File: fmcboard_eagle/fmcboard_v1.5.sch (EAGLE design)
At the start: 176 parts, among them IC1 OPA699ID, IC10 LTC6229IMS8E#TRPBF, IC11 7805TV, IC12 SN74AUC2G66DCTR, IC13 SN74AUC2G66DCTR, IC14 SN74AUC2G66DCTR, IC15 SN74AUC2G66DCTR, IC16 DAC7578SPWR, IC17 SN74AUC2G66DCTR, IC18 SN74AUC2G66DCTR, IC19 SN74AUC2G66DCTR, IC2 DAC7578SPWR, IC20 SN74AUC2G66DCTR, IC21 74AUP2GU04GW,125, IC22 74AUP2GU04GW,125, IC23 74AUP2GU04GW,125, IC24 74AUP2GU04GW,125, IC25 LM358, IC3 LTC6229IMS8E#TRPBF, IC4 LTC6229IMS8E#TRPBF, IC6 OPA699ID, IC7 OPA699ID, IC8 LTC6229IMS8E#TRPBF, IC9 LTC6229IMS8E#TRPBF, J1 8pin, J10 8pin, J12 4p-2.54, J2 ASP-134604-01, J3 4p-2.54, J4 4p-2.54, J5 8pin, J6 4p-2.54, J7 4p-2.54, J8 4p-2.54, J9 8pin, U1 TXS0108EPWR, U2 STMICROELECTRONICS_L7905ACVST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

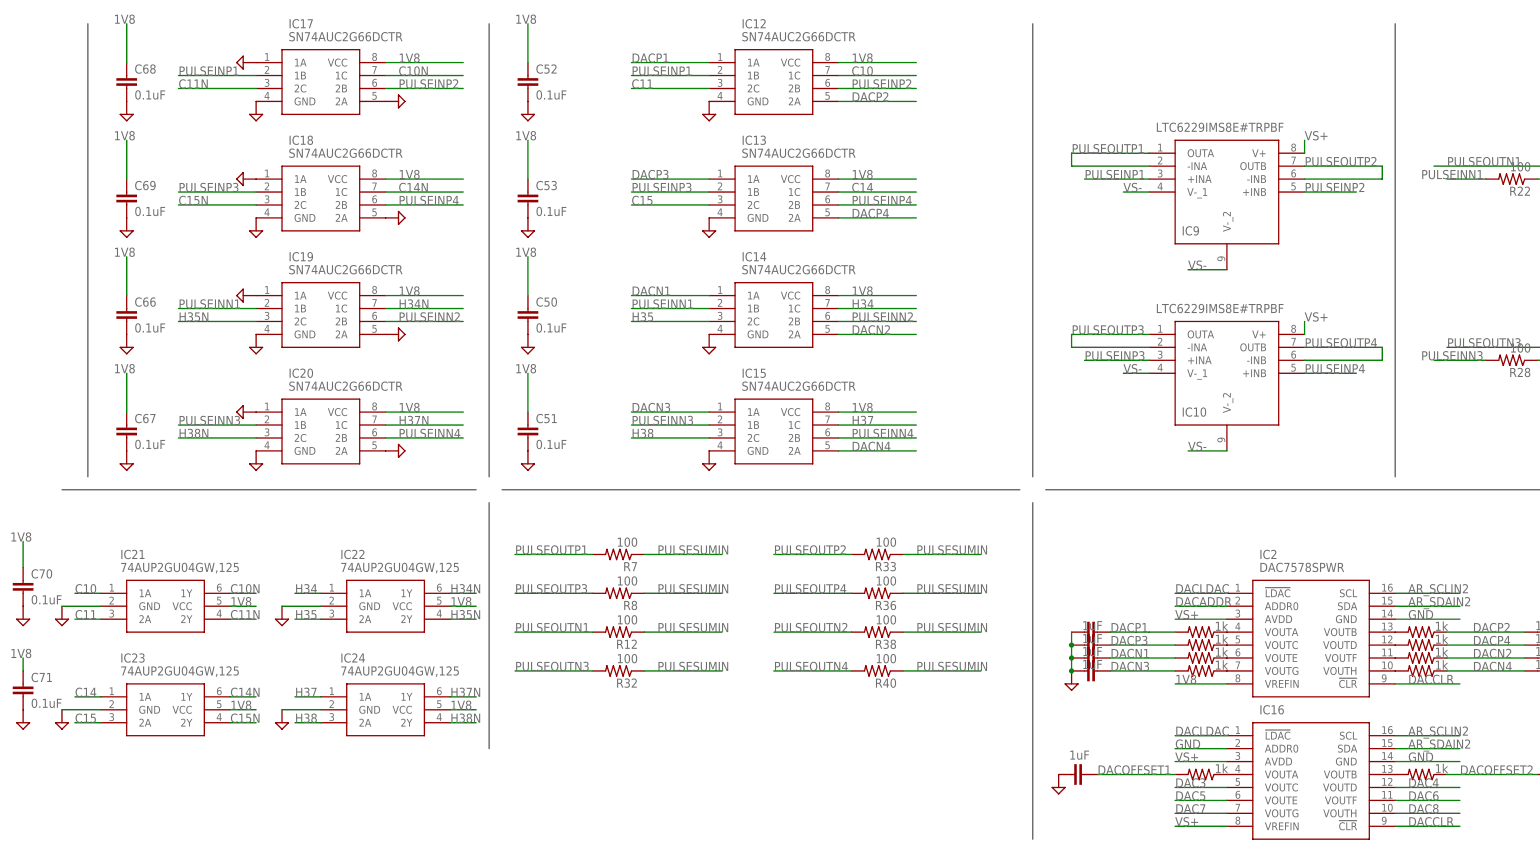
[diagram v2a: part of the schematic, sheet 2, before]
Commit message: 100 ohm between dac and caps
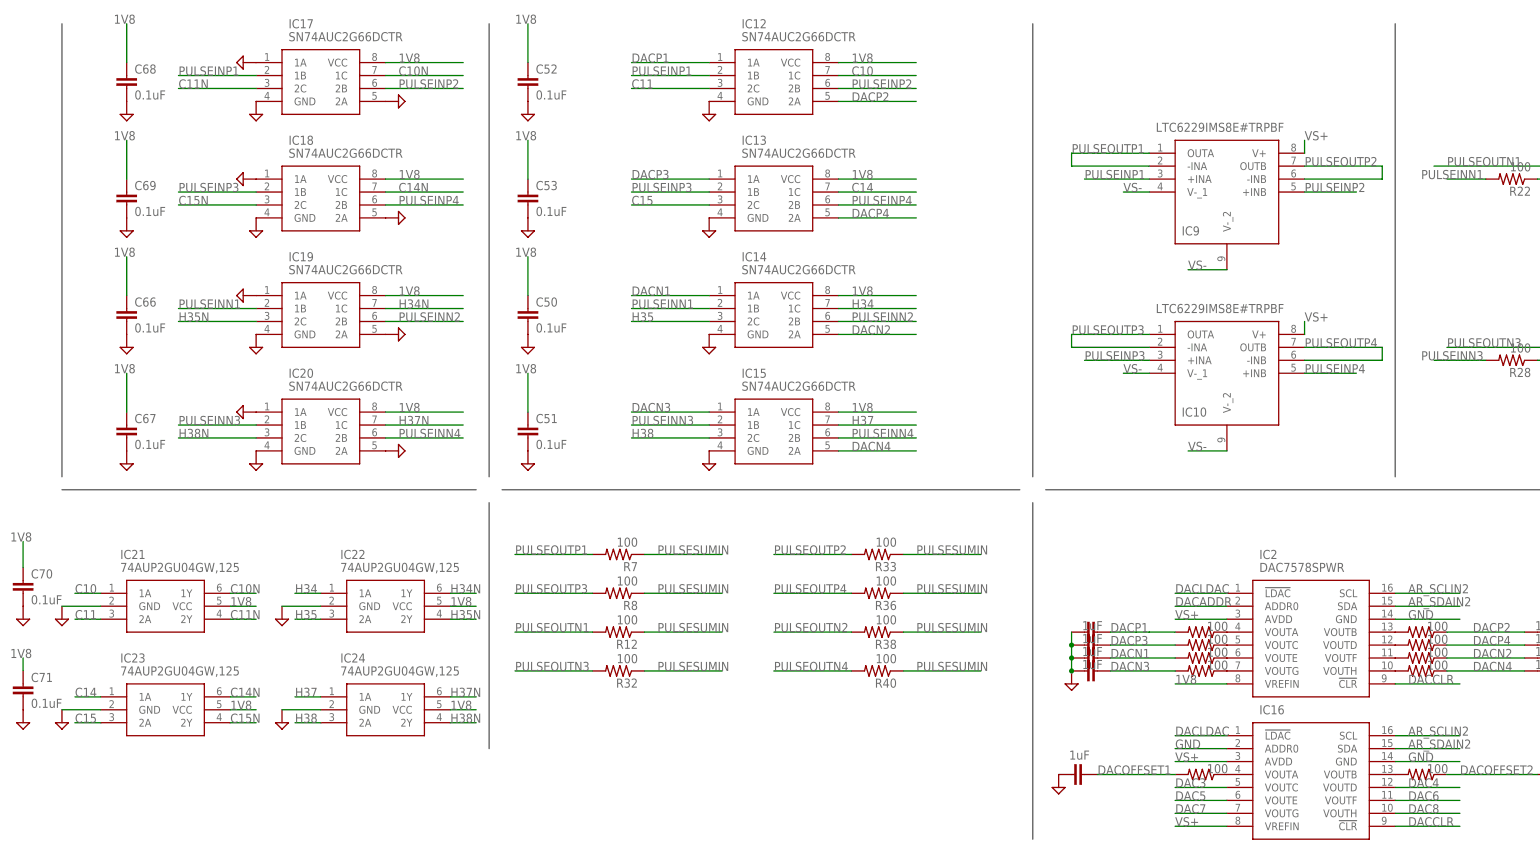
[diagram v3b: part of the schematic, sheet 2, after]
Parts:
- R47, R53, R54, R55, R56, R57, R58, R59, R60, R61: value 1k -> 100
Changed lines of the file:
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@@
 <part name="SUPPLY92" library="supply2" library_urn="urn:adsk.eagle:library:372" deviceset="GND" device=""/>
 <part name="IC25" library="SparkFun-IC-Amplifiers" library_urn="urn:adsk.eagle:library:520" deviceset="OPAMP-DUAL" device="U" package3d_urn="urn:adsk.eagle:package:38665/1" value="LM358"/>
-<part name="R47" library="rcl" library_urn="urn:adsk.eagle:library:334" deviceset="R-US_" device="R0805" package3d_urn="urn:adsk.eagle:package:23553/2" value="1k"/>
-<part name="R53" library="rcl" library_urn="urn:adsk.eagle:library:334" deviceset="R-US_" device="R0805" package3d_urn="urn:adsk.eagle:package:23553/2" value="1k"/>
-<part name="R54" library="rcl" library_urn="urn:adsk.eagle:library:334" deviceset="R-US_" device="R0805" package3d_urn="urn:adsk.eagle:package:23553/2" value="1k"/>
-<part name="R55" library="rcl" library_urn="urn:adsk.eagle:library:334" deviceset="R-US_" device="R0805" package3d_urn="urn:adsk.eagle:package:23553/2" value="1k"/>
-<part name="R56" library="rcl" library_urn="urn:adsk.eagle:library:334" deviceset="R-US_" device="R0805" package3d_urn="urn:adsk.eagle:package:23553/2" value="1k"/>
-<part name="R57" library="rcl" library_urn="urn:adsk.eagle:library:334" deviceset="R-US_" device="R0805" package3d_urn="urn:adsk.eagle:package:23553/2" value="1k"/>
-<part name="R58" library="rcl" library_urn="urn:adsk.eagle:library:334" deviceset="R-US_" device="R0805" package3d_urn="urn:adsk.eagle:package:23553/2" value="1k"/>
-<part name="R59" library="rcl" library_urn="urn:adsk.eagle:library:334" deviceset="R-US_" device="R0805" package3d_urn="urn:adsk.eagle:package:23553/2" value="1k"/>
-<part name="R60" library="rcl" library_urn="urn:adsk.eagle:library:334" deviceset="R-US_" device="R0805" package3d_urn="urn:adsk.eagle:package:23553/2" value="1k"/>
-<part name="R61" library="rcl" library_urn="urn:adsk.eagle:library:334" deviceset="R-US_" device="R0805" package3d_urn="urn:adsk.eagle:package:23553/2" value="1k"/>
+<part name="R47" library="rcl" library_urn="urn:adsk.eagle:library:334" deviceset="R-US_" device="R0805" package3d_urn="urn:adsk.eagle:package:23553/2" value="100"/>
+<part name="R53" library="rcl" library_urn="urn:adsk.eagle:library:334" deviceset="R-US_" device="R0805" package3d_urn="urn:adsk.eagle:package:23553/2" value="100"/>
+<part name="R54" library="rcl" library_urn="urn:adsk.eagle:library:334" deviceset="R-US_" device="R0805" package3d_urn="urn:adsk.eagle:package:23553/2" value="100"/>
+<part name="R55" library="rcl" library_urn="urn:adsk.eagle:library:334" deviceset="R-US_" device="R0805" package3d_urn="urn:adsk.eagle:package:23553/2" value="100"/>
+<part name="R56" library="rcl" library_urn="urn:adsk.eagle:library:334" deviceset="R-US_" device="R0805" package3d_urn="urn:adsk.eagle:package:23553/2" value="100"/>
+<part name="R57" library="rcl" library_urn="urn:adsk.eagle:library:334" deviceset="R-US_" device="R0805" package3d_urn="urn:adsk.eagle:package:23553/2" value="100"/>
+<part name="R58" library="rcl" library_urn="urn:adsk.eagle:library:334" deviceset="R-US_" device="R0805" package3d_urn="urn:adsk.eagle:package:23553/2" value="100"/>
+<part name="R59" library="rcl" library_urn="urn:adsk.eagle:library:334" deviceset="R-US_" device="R0805" package3d_urn="urn:adsk.eagle:package:23553/2" value="100"/>
+<part name="R60" library="rcl" library_urn="urn:adsk.eagle:library:334" deviceset="R-US_" device="R0805" package3d_urn="urn:adsk.eagle:package:23553/2" value="100"/>
+<part name="R61" library="rcl" library_urn="urn:adsk.eagle:library:334" deviceset="R-US_" device="R0805" package3d_urn="urn:adsk.eagle:package:23553/2" value="100"/>
 </parts>
 <sheets>
@@
 <wire x1="12.7" y1="30.48" x2="12.7" y2="119.38" width="0.1524" layer="97"/>
 <text x="-15.24" y="119.38" size="1.778" layer="90">Pulse switches to gnd</text>
-<wire x1="-66.04" y1="30.48" x2="-66.04" y2="119.38" width="0.1524" layer="97"/>
+<wire x1="-71.12" y1="30.48" x2="-71.12" y2="119.38" width="0.1524" layer="97"/>
 <text x="-63.5" y="22.86" size="1.778" layer="90">Inverters for pulse switches to DACs</text>
 <wire x1="12.7" y1="-22.86" x2="12.7" y2="25.4" width="0.1524" layer="97"/>

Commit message: routed
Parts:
- added J11: 8pin, SparkFun-Connectors:CONN_08"
- renumbered IO_G2 to IO_C10, IO_G3 to IO_H34
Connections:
- removed net G2: IO_C10.1, J2.G2, R4.2
- removed net G3: IO_H34.1, J2.G3, R5.2
- net C10: now also IO_C10.1, R4.2
- net GND: now also J11.1, J11.2, J11.3, J11.4, J11.5, J11.6, J11.7, J11.8
- net H34: now also IO_H34.1, R5.2
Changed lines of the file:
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@@
 <class number="1" name="power" width="0.4064" drill="0">
 </class>
-<class number="2" name="gnd" width="0.3048" drill="0">
-</class>
 </classes>
 <parts>
@@
 <part name="R_O1" library="resistor" library_urn="urn:adsk.eagle:library:348" deviceset="R-TRIMM" device="3296W" package3d_urn="urn:adsk.eagle:package:26033/1" value="5k"/>
 <part name="R3" library="rcl" library_urn="urn:adsk.eagle:library:334" deviceset="R-US_" device="R0805" package3d_urn="urn:adsk.eagle:package:23553/2" value="100k"/>
-<part name="IO_G2" library="con-coax" library_urn="urn:adsk.eagle:library:133" deviceset="BU-SMB-V" device="" package3d_urn="urn:adsk.eagle:package:6209/1"/>
-<part name="IO_G3" library="con-coax" library_urn="urn:adsk.eagle:library:133" deviceset="BU-SMB-V" device="" package3d_urn="urn:adsk.eagle:package:6209/1"/>
+<part name="IO_C10" library="con-coax" library_urn="urn:adsk.eagle:library:133" deviceset="BU-SMB-V" device="" package3d_urn="urn:adsk.eagle:package:6209/1"/>
+<part name="IO_H34" library="con-coax" library_urn="urn:adsk.eagle:library:133" deviceset="BU-SMB-V" device="" package3d_urn="urn:adsk.eagle:package:6209/1"/>
 <part name="IO_H4" library="con-coax" library_urn="urn:adsk.eagle:library:133" deviceset="BU-SMB-V" device="" package3d_urn="urn:adsk.eagle:package:6209/1"/>
 <part name="IO_H5" library="con-coax" library_urn="urn:adsk.eagle:library:133" deviceset="BU-SMB-V" device="" package3d_urn="urn:adsk.eagle:package:6209/1"/>
@@
 <part name="R60" library="rcl" library_urn="urn:adsk.eagle:library:334" deviceset="R-US_" device="R0805" package3d_urn="urn:adsk.eagle:package:23553/2" value="100"/>
 <part name="R61" library="rcl" library_urn="urn:adsk.eagle:library:334" deviceset="R-US_" device="R0805" package3d_urn="urn:adsk.eagle:package:23553/2" value="100"/>
+<part name="J11" library="SparkFun-Connectors" library_urn="urn:adsk.eagle:library:513" deviceset="CONN_08" device="&quot;" package3d_urn="urn:adsk.eagle:package:38138/1" value="8pin"/>
+<part name="SUPPLY93" library="supply2" library_urn="urn:adsk.eagle:library:372" deviceset="GND" device=""/>
 </parts>
 <sheets>
@@
 <attribute name="NAME" x="-30.48" y="104.14" size="1.778" layer="95" rot="R180"/>
 </instance>
-<instance part="IO_G2" gate="G1" x="53.34" y="99.06" smashed="yes">
+<instance part="IO_C10" gate="G1" x="53.34" y="99.06" smashed="yes">
 <attribute name="NAME" x="48.26" y="102.362" size="1.778" layer="95"/>
 </instance>
-<instance part="IO_G3" gate="G1" x="53.34" y="88.9" smashed="yes">
+<instance part="IO_H34" gate="G1" x="53.34" y="88.9" smashed="yes">
 <attribute name="NAME" x="48.26" y="92.202" size="1.778" layer="95"/>
 </instance>
@@
 <attribute name="VALUE" x="1.524" y="13.081" size="1.778" layer="96"/>
 </instance>
+<instance part="J11" gate="G$1" x="99.06" y="111.76" smashed="yes" rot="R180"/>
+<instance part="SUPPLY93" gate="GND" x="93.98" y="99.06" smashed="yes"/>
 </instances>
 <busses>
 </busses>
 <nets>
-<net name="GND" class="2">
+<net name="GND" class="0">
 <segment>
 <pinref part="J4" gate="G$1" pin="P$4"/>
@@
 </segment>
 <segment>
-<pinref part="IO_G3" gate="G1" pin="2"/>
+<pinref part="IO_H34" gate="G1" pin="2"/>
 <pinref part="SUPPLY27" gate="GND" pin="GND"/>
 <pinref part="R5" gate="G$1" pin="1"/>
@@
 </segment>
 <segment>
-<pinref part="IO_G2" gate="G1" pin="2"/>
+<pinref part="IO_C10" gate="G1" pin="2"/>
 <pinref part="SUPPLY28" gate="GND" pin="GND"/>
 <pinref part="R4" gate="G$1" pin="1"/>
@@
 <label x="121.92" y="25.4" size="1.778" layer="95"/>
 </segment>
+<segment>
+<pinref part="J11" gate="G$1" pin="1"/>
+<pinref part="J11" gate="G$1" pin="2"/>
+<wire x1="93.98" y1="119.38" x2="93.98" y2="116.84" width="0.1524" layer="91"/>
+<pinref part="J11" gate="G$1" pin="3"/>
+<wire x1="93.98" y1="116.84" x2="93.98" y2="114.3" width="0.1524" layer="91"/>
+<junction x="93.98" y="116.84"/>
+<pinref part="J11" gate="G$1" pin="4"/>
+<wire x1="93.98" y1="114.3" x2="93.98" y2="111.76" width="0.1524" layer="91"/>
+<junction x="93.98" y="114.3"/>
+<pinref part="J11" gate="G$1" pin="5"/>
+<wire x1="93.98" y1="111.76" x2="93.98" y2="109.22" width="0.1524" layer="91"/>
+<junction x="93.98" y="111.76"/>
+<pinref part="J11" gate="G$1" pin="6"/>
+<wire x1="93.98" y1="109.22" x2="93.98" y2="106.68" width="0.1524" layer="91"/>
+<junction x="93.98" y="109.22"/>
+<pinref part="J11" gate="G$1" pin="7"/>
+<wire x1="93.98" y1="106.68" x2="93.98" y2="104.14" width="0.1524" layer="91"/>
+<junction x="93.98" y="106.68"/>
+<pinref part="J11" gate="G$1" pin="8"/>
+<wire x1="93.98" y1="104.14" x2="93.98" y2="101.6" width="0.1524" layer="91"/>
+<junction x="93.98" y="104.14"/>
+<pinref part="SUPPLY93" gate="GND" pin="GND"/>
+<junction x="93.98" y="101.6"/>
+</segment>
 </net>
 <net name="IO1" class="0">
@@
 </segment>
 </net>
-<net name="G2" class="0">
-<segment>
-<pinref part="IO_G2" gate="G1" pin="1"/>
-<wire x1="55.88" y1="99.06" x2="43.18" y2="99.06" width="0.1524" layer="91"/>
-<label x="43.18" y="99.06" size="1.778" layer="95"/>
-<pinref part="R4" gate="G$1" pin="2"/>
-<junction x="55.88" y="99.06"/>
-</segment>
-</net>
-<net name="G3" class="0">
-<segment>
-<pinref part="IO_G3" gate="G1" pin="1"/>
-<wire x1="55.88" y1="88.9" x2="43.18" y2="88.9" width="0.1524" layer="91"/>
-<label x="43.18" y="88.9" size="1.778" layer="95"/>
-<pinref part="R5" gate="G$1" pin="2"/>
-<junction x="55.88" y="88.9"/>
-</segment>
-</net>
 <net name="G36" class="0">
 <segment>
@@
 </segment>
 </net>
+<net name="C10" class="0">
+<segment>
+<pinref part="IO_C10" gate="G1" pin="1"/>
+<wire x1="55.88" y1="99.06" x2="43.18" y2="99.06" width="0.1524" layer="91"/>
+<label x="43.18" y="99.06" size="1.778" layer="95"/>
+<pinref part="R4" gate="G$1" pin="2"/>
+<junction x="55.88" y="99.06"/>
+</segment>
+</net>
+<net name="H34" class="0">
+<segment>
+<pinref part="IO_H34" gate="G1" pin="1"/>
+<wire x1="55.88" y1="88.9" x2="43.18" y2="88.9" width="0.1524" layer="91"/>
+<label x="43.18" y="88.9" size="1.778" layer="95"/>
+<pinref part="R5" gate="G$1" pin="2"/>
+<junction x="55.88" y="88.9"/>
+</segment>
+</net>
 </nets>
 </sheet>
@@
 </busses>
 <nets>
-<net name="GND" class="2">
+<net name="GND" class="0">
 <segment>
 <wire x1="233.68" y1="86.36" x2="223.52" y2="86.36" width="0.1524" layer="91"/>
@@
 </busses>
 <nets>
-<net name="GND" class="2">
+<net name="GND" class="0">
 <segment>
 <pinref part="SUPPLY1" gate="GND" pin="GND"/>
@@
 </busses>
 <nets>
-<net name="GND" class="2">
+<net name="GND" class="0">
 <segment>
 <pinref part="J2" gate="G$1" pin="H6"/>
@@
 </segment>
 </net>
-<net name="G2" class="0">
-<segment>
-<pinref part="J2" gate="G$1" pin="G2"/>
-<wire x1="48.26" y1="7.62" x2="33.02" y2="7.62" width="0.1524" layer="91"/>
-<label x="35.56" y="7.62" size="1.778" layer="95"/>
-</segment>
-</net>
-<net name="G3" class="0">
-<segment>
-<pinref part="J2" gate="G$1" pin="G3"/>
-<wire x1="33.02" y1="10.16" x2="48.26" y2="10.16" width="0.1524" layer="91"/>
-<label x="35.56" y="10.16" size="1.778" layer="95"/>
-</segment>
-</net>

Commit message: v1.51
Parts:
- C32, C33: value 1pF -> 1pF?
- IC21, IC22, IC23, IC24: value 74AUP2GU04GW,125 -> 74AUP2GU04GW; MANUFACTURER_PART_NUMBER (none) -> 74AUP2GU04GW
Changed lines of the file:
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@@
 <part name="C36" library="SparkFun-Passives" deviceset="CAP" device="0805" value="1pF"/>
 <part name="C37" library="SparkFun-Passives" deviceset="CAP" device="0805" value="1pF"/>
-<part name="C32" library="SparkFun-Passives" deviceset="CAP" device="0805" value="1pF"/>
-<part name="C33" library="SparkFun-Passives" deviceset="CAP" device="0805" value="1pF"/>
+<part name="C32" library="SparkFun-Passives" deviceset="CAP" device="0805" value="1pF?"/>
+<part name="C33" library="SparkFun-Passives" deviceset="CAP" device="0805" value="1pF?"/>
 <part name="R34" library="rcl" library_urn="urn:adsk.eagle:library:334" deviceset="R-US_" device="R0805" package3d_urn="urn:adsk.eagle:package:23553/2" value="47"/>
 <part name="R42" library="rcl" library_urn="urn:adsk.eagle:library:334" deviceset="R-US_" device="R0805" package3d_urn="urn:adsk.eagle:package:23553/2" value="50?"/>
@@
 <part name="SUPPLY81" library="supply2" library_urn="urn:adsk.eagle:library:372" deviceset="GND" device=""/>
 <part name="SUPPLY82" library="supply2" library_urn="urn:adsk.eagle:library:372" deviceset="GND" device=""/>
-<part name="IC21" library="74AUP2GU04GW_125" deviceset="74AUP2GU04GW,125" device=""/>
-<part name="IC22" library="74AUP2GU04GW_125" deviceset="74AUP2GU04GW,125" device=""/>
-<part name="IC23" library="74AUP2GU04GW_125" deviceset="74AUP2GU04GW,125" device=""/>
-<part name="IC24" library="74AUP2GU04GW_125" deviceset="74AUP2GU04GW,125" device=""/>
+<part name="IC21" library="74AUP2GU04GW_125" deviceset="74AUP2GU04GW,125" device="" value="74AUP2GU04GW">
+<attribute name="MANUFACTURER_PART_NUMBER" value="74AUP2GU04GW"/>
+</part>
+<part name="IC22" library="74AUP2GU04GW_125" deviceset="74AUP2GU04GW,125" device="" value="74AUP2GU04GW">
+<attribute name="MANUFACTURER_PART_NUMBER" value="74AUP2GU04GW"/>
+</part>
+<part name="IC23" library="74AUP2GU04GW_125" deviceset="74AUP2GU04GW,125" device="" value="74AUP2GU04GW">
+<attribute name="MANUFACTURER_PART_NUMBER" value="74AUP2GU04GW"/>
+</part>
+<part name="IC24" library="74AUP2GU04GW_125" deviceset="74AUP2GU04GW,125" device="" value="74AUP2GU04GW">
+<attribute name="MANUFACTURER_PART_NUMBER" value="74AUP2GU04GW"/>
+</part>
 <part name="SUPPLY83" library="supply2" library_urn="urn:adsk.eagle:library:372" deviceset="GND" device=""/>
 <part name="SUPPLY84" library="supply2" library_urn="urn:adsk.eagle:library:372" deviceset="GND" device=""/>
